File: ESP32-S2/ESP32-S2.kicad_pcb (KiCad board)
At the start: 2 copper layers, 27.9 x 70 mm, 39 parts, among them J1 Conn_01x18_Male, J2 Conn_01x21_Male, J3 USB_A, J4 TYPE-C-31-M-12, Q2 L8050QLT1G, Q3 L8050QLT1G, SW1 SW_Push, SW2 SW_Push, U2 ESP32-S2-WROOM-ESP32-S2-WROOM, U3 AMS1117-3.3, U4 CH340C

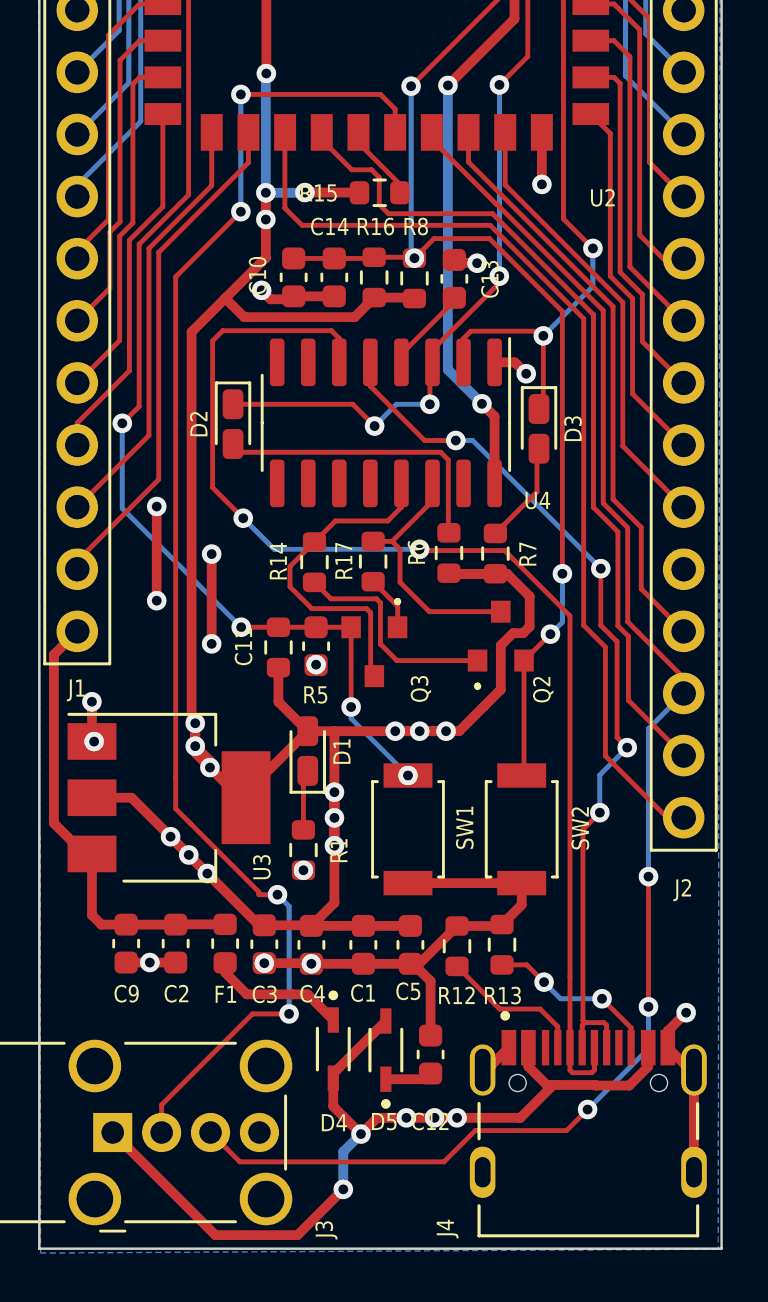
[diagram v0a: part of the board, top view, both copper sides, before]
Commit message: Silkscreen Modified
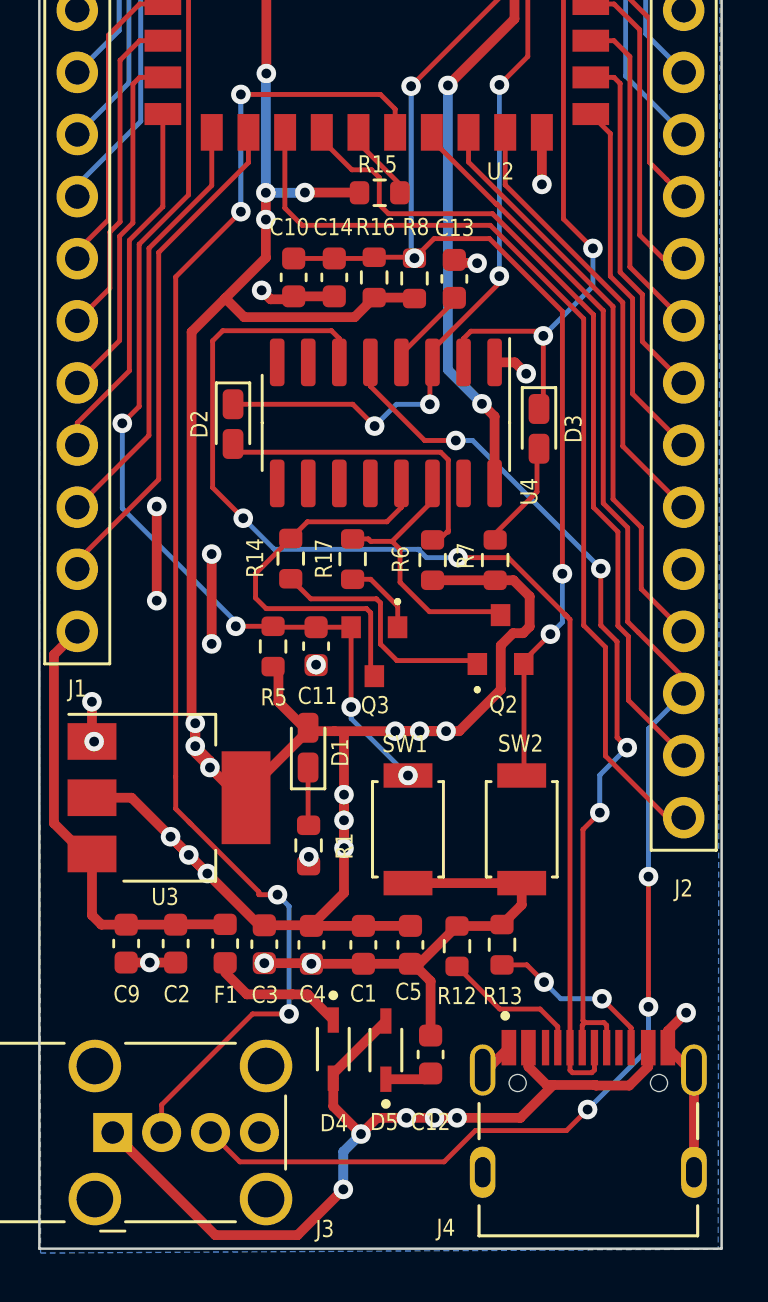
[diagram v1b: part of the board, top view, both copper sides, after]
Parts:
- moved R14 0.98 mm to (147.2, 108.9)
- moved R17 0.85 mm to (149.7, 108.9)
- moved R6 0.73 mm to (153.0, 108.9)
- moved R1 0.28 mm to (147.9, 120.6)
- moved R7 0.27 mm to (155.5, 108.9)
- moved R5 0.22 mm to (146.5, 112.5)
- moved D1 0.14 mm to (147.9, 116.6)
- moved Q2 0.14 mm to (155.8, 112.2)
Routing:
- net /~DTR: track 13.8 -> 16.7 mm
- net +3V3: track 124.5 -> 122.9 mm
- net Net-(Q2-Pad1): track 8.98 -> 10.0 mm
- net Net-(Q3-Pad1): track 2.27 -> 3.15 mm
- net /~RTS: track 10.3 -> 11.1 mm
- net Net-(D2-Pad2): track 12.1 -> 12.8 mm

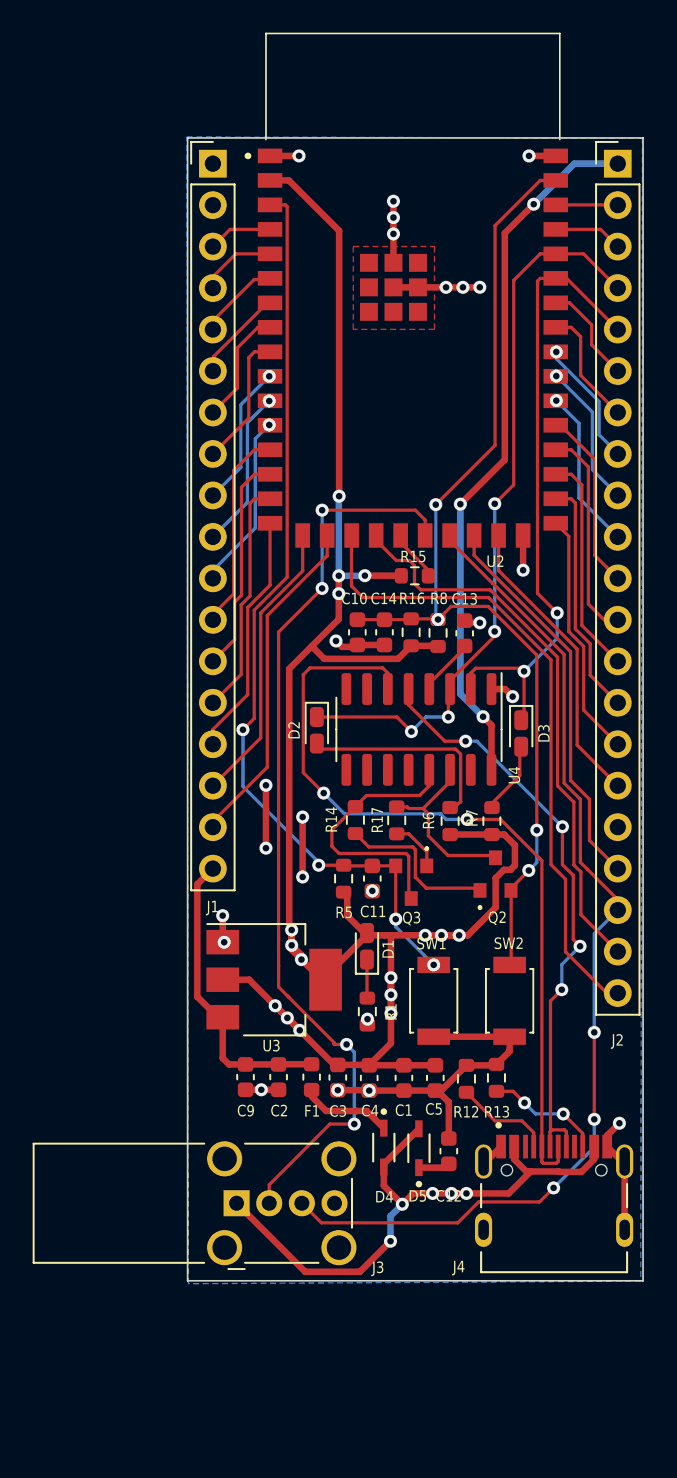
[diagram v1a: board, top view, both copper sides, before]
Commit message: Changes in Routing and Silkscreen
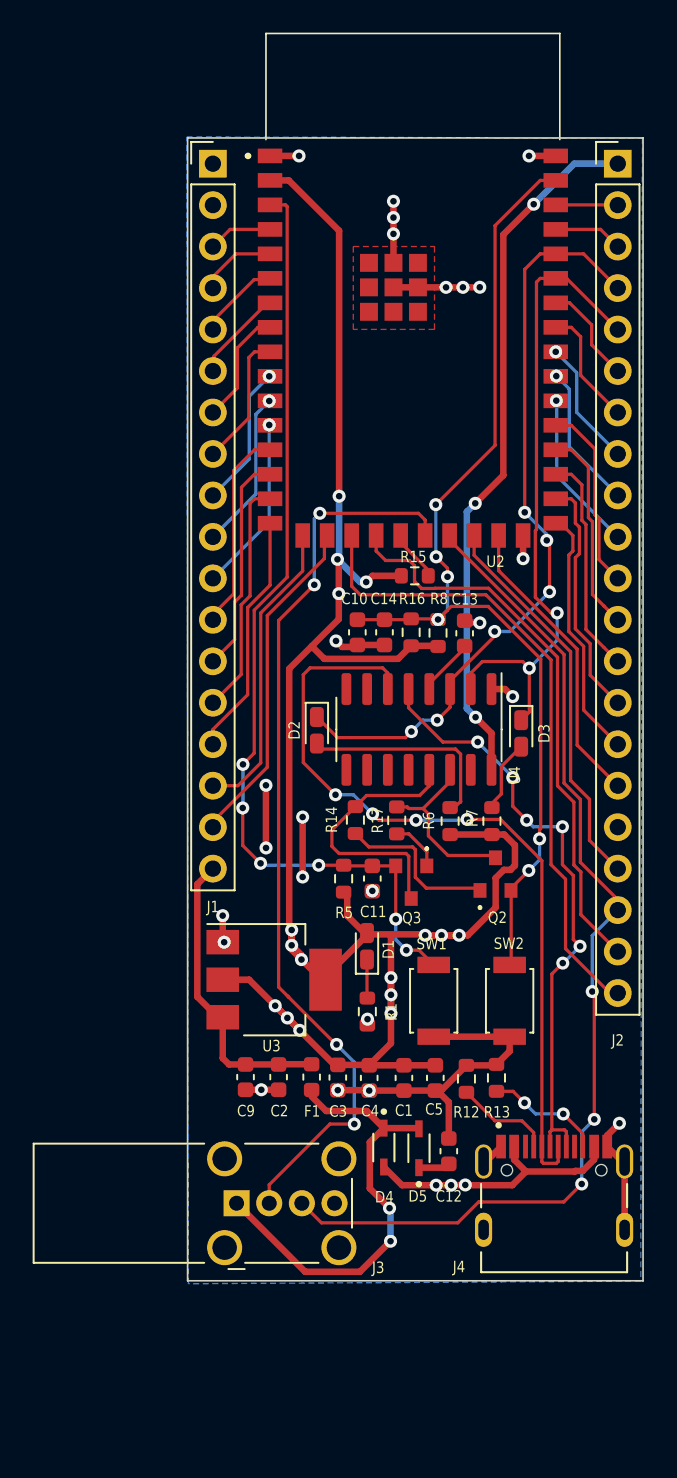
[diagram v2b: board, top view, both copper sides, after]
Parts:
- added REF**: OSHW-Logo2_9.8x8mm_SilkScreen, Symbol:OSHW-Logo2_9.8x8mm_SilkScreen, B.Cu at (156.3, 72.8)
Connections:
- D4 pad A: /VBUS -> /VBUSC
- D4 pad C: Net-(D4-PadC) -> /VBUS
- F1 pad 2: Net-(D4-PadC) -> /VBUS
- J1 pad 2: /3V3 -> (no net)
- J4 pad A4B9: /VBUS -> /VBUSC
- J4 pad A8: Net-(J4-PadA8) -> (no net)
- J4 pad B4A9: /VBUS -> /VBUSC
- J4 pad B8: Net-(J4-PadB8) -> (no net)
- U4 pad 10: Net-(U4-Pad10) -> (no net)
- U4 pad 11: Net-(U4-Pad11) -> (no net)
- U4 pad 12: Net-(U4-Pad12) -> (no net)
- U4 pad 15: Net-(U4-Pad15) -> (no net)
- U4 pad 7: Net-(U4-Pad7) -> (no net)
- U4 pad 8: Net-(U4-Pad8) -> (no net)
- U4 pad 9: Net-(U4-Pad9) -> (no net)
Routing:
- net /VBUSC: track 0.00 -> 17.5 mm, vias 0 -> 3
- net /VBUS: track 37.0 -> 27.1 mm, vias 5 -> 2
- net Net-(D4-PadC): track 5.22 -> 0.00 mm
- net /GPIO0: track 56.1 -> 58.5 mm, vias 4 -> 6
- net /RXD0: track 45.4 -> 47.2 mm, vias 4 -> 6
- net /DP1: track 36.9 -> 38.0 mm, vias 4 -> 6
- net /GPIO20: track 62.7 -> 63.6 mm
- net +3V3: track 122.9 -> 123.8 mm
- net /TXD0: track 39.7 -> 40.6 mm
- net /GPIO14: track 17.6 -> 18.5 mm
- net /CHIP_PU: track 62.9 -> 63.8 mm, vias 4 -> 6
- net GND: track 61.7 -> 61.0 mm
- net /GPIO19: track 56.6 -> 56.0 mm
- net /DN1: track 50.3 -> 49.9 mm, vias 2 -> 4

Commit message: optimised routing
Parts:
- moved J3 3.08 mm to (141.9, 134.7), turned to 90 degrees
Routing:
- net /GPIO20: track 63.6 -> 73.8 mm
- net /VBUS: track 27.1 -> 17.3 mm, vias 2 -> 0
- net GND: track 61.0 -> 54.0 mm, vias 24 -> 22
- net +3V3: track 123.8 -> 119.0 mm, vias 16 -> 4
- net /SCL: track 7.80 -> 12.1 mm
- net /GPIO39: track 8.85 -> 12.6 mm
- net /GPIO38: track 9.89 -> 13.5 mm
- net /GPIO9: track 10.8 -> 14.0 mm
- net /GPIO8: track 9.75 -> 12.7 mm
- net /GPIO7: track 8.88 -> 11.3 mm
- net /RXD0: track 47.2 -> 49.4 mm
- net /GPIO0: track 58.5 -> 60.5 mm
- net /TXD0: track 40.6 -> 42.4 mm
- net /VBUSC: track 17.5 -> 18.5 mm, vias 3 -> 0

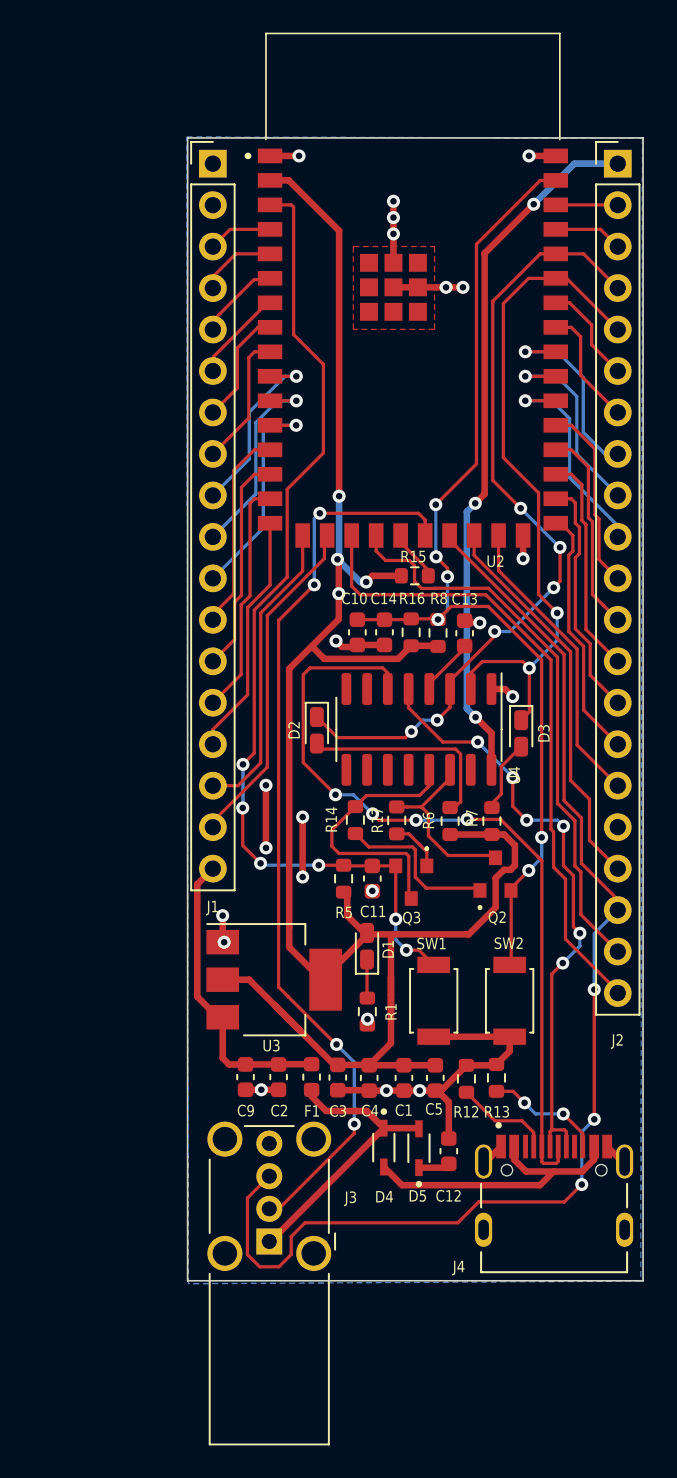
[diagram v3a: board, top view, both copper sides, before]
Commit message: made changes- routing and schematic, added silk screen- pin headers
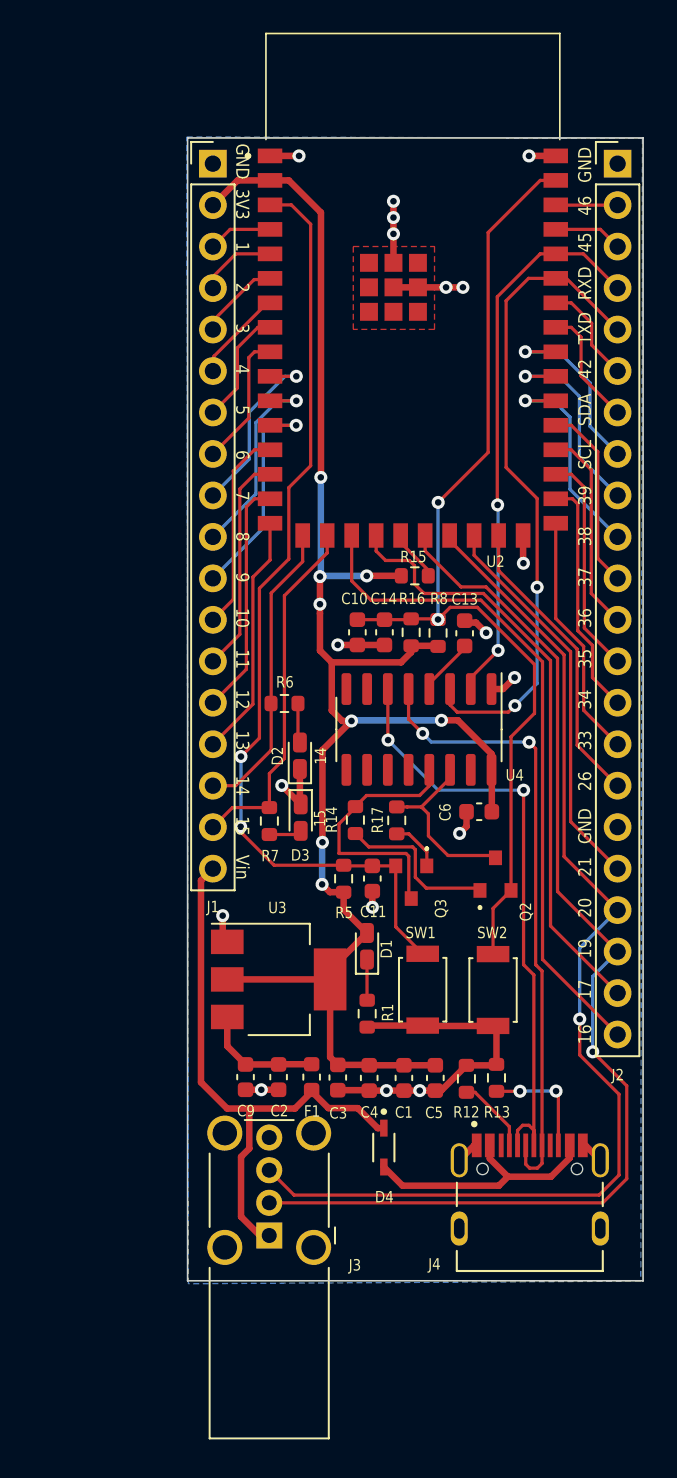
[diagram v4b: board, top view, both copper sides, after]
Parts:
- removed C12: 0.1uF, Capacitor_SMD:C_0603_1608Metric
- removed D5: BAT760-7, BAT-760:SOD2513X120N
- removed the REF** at (156.3, 72.8)
- added C6: 0.1uF, Capacitor_SMD:C_0603_1608Metric, F.Cu at (154.8, 108.4)
- added REF**: KiCad-Logo2_5mm_SilkScreen, Symbol:KiCad-Logo2_5mm_SilkScreen, B.Cu at (154.6, 70.8)
- added REF**: OSHW-Logo2_7.3x6mm_SilkScreen, Symbol:OSHW-Logo2_7.3x6mm_SilkScreen, B.Cu at (144.1, 71.2)
- C13: value 10nF -> 0.1uF
- J2: value Conn_01x21_Male -> Conn_01x22_Male; footprint Connector_PinHeader_2.54mm:PinHeader_1x21_P2.54mm_Vertical -> Connector_PinHeader_2.54mm:PinHeader_1x22_P2.54mm_Vertical
- moved D3 14.5 mm to (143.8, 108.7)
- moved R7 13.6 mm to (141.9, 108.9), turned to 270 degrees
- moved R6 12.4 mm to (142.8, 101.7), turned to 0 degrees
- moved D2 1.87 mm to (143.8, 104.9), turned to 90 degrees
- moved J4 1.49 mm to (157.9, 133.9)
- moved SW2 1.21 mm to (155.6, 119.3)
- moved SW1 0.96 mm to (151.3, 119.3)
- moved J3 0.37 mm to (141.9, 134.3)
- moved U3 0.28 mm to (142.5, 118.6)
- moved R1 0.13 mm to (147.9, 120.7)
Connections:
- D2 pad 1: /RXD0 -> GND
- D3 pad 1: /TXD0 -> GND
- D4 pad C: /VBUS -> /VBUSA
- F1 pad 2: /VBUS -> /VBUSA
- J1 pad 18: /VI -> /VBUSA
- J1 pad 2: (no net) -> +3V3
- J2 pad 1: VCC -> GND
- J2 pad 20: /GPIO17 -> /GPIO19
- J2 pad 21: /GPIO16 -> /GPIO17
- J3 pad 1: /VBUS -> /VBUSA
- J4 pad A8: (no net) -> Net-(J4-PadA8)
- J4 pad B8: (no net) -> Net-(J4-PadB8)
- R6 pad 1: +3V3 -> /GPIO14
- R7 pad 1: +3V3 -> /GPIO15
- U4 pad 10: (no net) -> Net-(U4-Pad10)
- U4 pad 11: (no net) -> Net-(U4-Pad11)
- U4 pad 12: (no net) -> Net-(U4-Pad12)
- U4 pad 15: (no net) -> Net-(U4-Pad15)
- U4 pad 16: VCC -> +3V3
- U4 pad 2: /TXD0 -> /RXD0
- U4 pad 3: /RXD0 -> /TXD0
- U4 pad 7: (no net) -> Net-(U4-Pad7)
- U4 pad 8: (no net) -> Net-(U4-Pad8)
- U4 pad 9: (no net) -> Net-(U4-Pad9)
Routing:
- net VCC: track 43.1 -> 0.00 mm, vias 3 -> 0
- net /VBUSA: track 0.00 -> 36.3 mm
- net /VBUS: track 17.3 -> 0.00 mm
- net +3V3: track 119.0 -> 104.1 mm, vias 4 -> 8
- net /RXD0: track 49.4 -> 34.6 mm, vias 6 -> 2
- net /GPIO19: track 55.8 -> 69.8 mm, vias 4 -> 1
- net /DN1: track 49.9 -> 38.2 mm, vias 4 -> 2
- net /VI: track 18.4 -> 7.73 mm
- net Net-(D2-Pad2): track 12.8 -> 2.44 mm
- net /GPIO20: track 73.8 -> 68.0 mm, vias 3 -> 1
- net /VBUSC: track 18.5 -> 15.9 mm
- net /GPIO0: track 60.5 -> 58.2 mm, vias 6 -> 2
- net /GPIO17: track 34.9 -> 37.2 mm
- net Net-(D3-Pad2): track 4.20 -> 2.01 mm
- net /GPIO16: track 39.3 -> 41.3 mm
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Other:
- board text added: "1"
- board text added: "10"
- board text added: "11"
- board text added: "12"
- board text added: "13"
- board text added: "14"
- board text added: "15"
- board text added: "16"
- board text added: "17"
- board text added: "19"
- board text added: "2"
- board text added: "20"
- board text added: "21"
- board text added: "26"
- board text added: "3"
- board text added: "33"
- board text added: "34"
- board text added: "35"
- board text added: "36"
- board text added: "37"
- board text added: "38"
- board text added: "39"
- board text added: "3V3"
- board text added: "4"
- board text added: "42"
- board text added: "45"
- board text added: "46"
- board text added: "5"
- board text added: "6"
- board text added: "7"
- board text added: "8"
- board text added: "9"
- board text added: "GND"
- board text added: "RXD"
- board text added: "SCL"
- board text added: "SDA"
- board text added: "TXD"
- board text added: "Vin"

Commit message: Changes in PCB
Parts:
- moved R13 3.83 mm to (159.6, 125.2)
- moved R12 2.72 mm to (156.7, 125.2)
- moved R6 1.00 mm to (143.8, 101.5), turned to 270 degrees
- moved C6 0.64 mm to (154.3, 108.8), turned to 270 degrees
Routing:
- net /GPIO15: track 22.6 -> 33.0 mm
- net /CC2: track 7.04 -> 2.80 mm, vias 2 -> 0
- net GND: track 53.5 -> 51.3 mm, vias 18 -> 21
- net /GPIO14: track 18.4 -> 20.3 mm
- net /CC1: track 4.65 -> 2.76 mm
- net +3V3: track 104.1 -> 103.2 mm
- net /DP1: track 39.0 -> 38.5 mm
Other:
- board text added: "BOOT"
- board text added: "EN"
- board text added: "PWR"
